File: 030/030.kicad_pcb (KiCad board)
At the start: 2 copper layers, 18 x 21.6 mm, 7 parts, among them J1 030

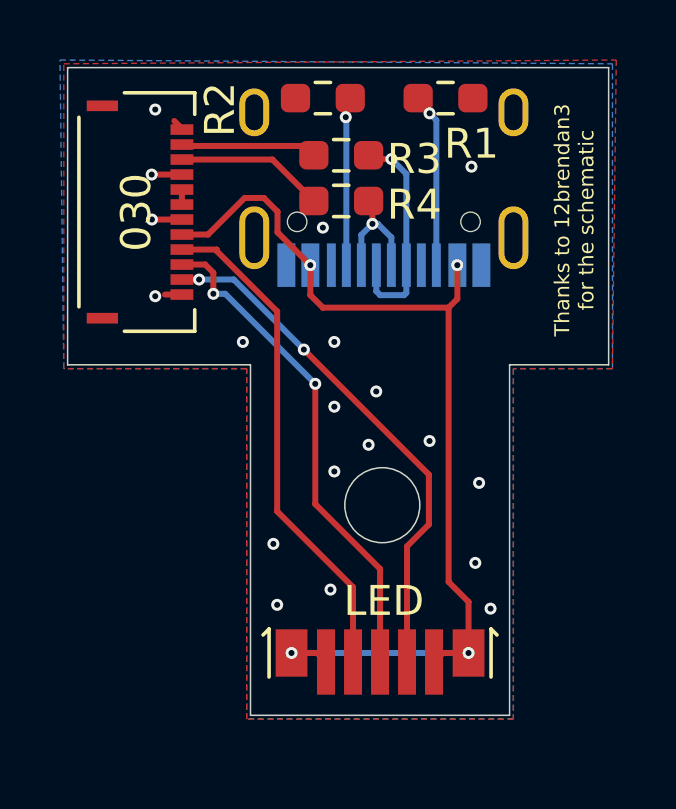
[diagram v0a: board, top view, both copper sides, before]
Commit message: update 030 to potentially correct schematic. Remove bad 001/011.
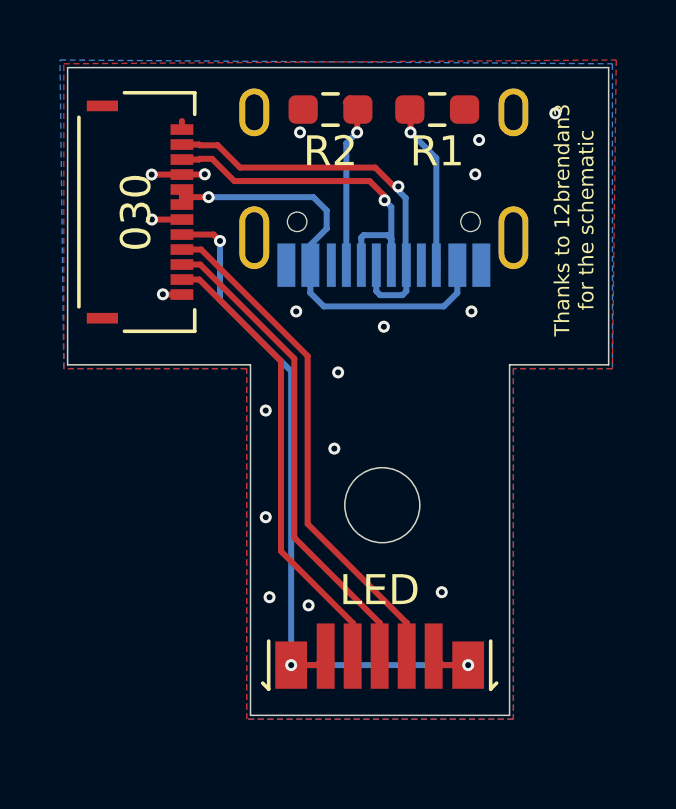
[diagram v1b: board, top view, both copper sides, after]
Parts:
- removed R3, R4: comp, Resistor_SMD:R_0603_1608Metric_Pad0.98x0.95mm_HandSolder
- moved R1 0.47 mm to (108.1, 53.7)
- moved R2 0.46 mm to (104.5, 53.7)
- moved D1 0.20 mm to (106.2, 71.9), turned to 180 degrees
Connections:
- D1 pad 1: +5V -> /Annode
- D1 pad 2: +5V -> /Annode
- D1 pad 6: +5V -> /Annode
- D1 pad 7: +5V -> /Annode
- J1 pad 5: Net-(J1-Pad5) -> +5V
- J1 pad 6: Net-(J1-Pad5) -> +5V
- J1 pad 8: +5V -> /Annode
- USB pad A6: Net-(J2-PadA6) -> /D+
- USB pad A7: Net-(J2-PadA7) -> /D-
- USB pad B6: Net-(J2-PadA6) -> /D+
- USB pad B7: Net-(J2-PadA7) -> /D-
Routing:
- net /Annode: track 0.00 -> 24.9 mm, vias 0 -> 3
- net +5V: track 33.7 -> 14.9 mm, vias 4 -> 1
- net /D+: track 4.55 -> 13.4 mm, vias 0 -> 1
- net /D-: track 4.97 -> 12.6 mm, vias 0 -> 1
- net Net-(J2-PadA6): track 7.44 -> 0.00 mm, vias 1 -> 0
- net Net-(J2-PadA7): track 4.11 -> 0.00 mm, vias 1 -> 0
- net /B: track 17.5 -> 15.5 mm, vias 2 -> 0
- net GND: track 2.96 -> 3.73 mm, vias 19 -> 18
- net Net-(J1-Pad5): track 0.50 -> 0.00 mm
- net /R: track 16.7 -> 16.3 mm, vias 2 -> 0

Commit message: 001, 011, 030 standardized to a cheaper LED
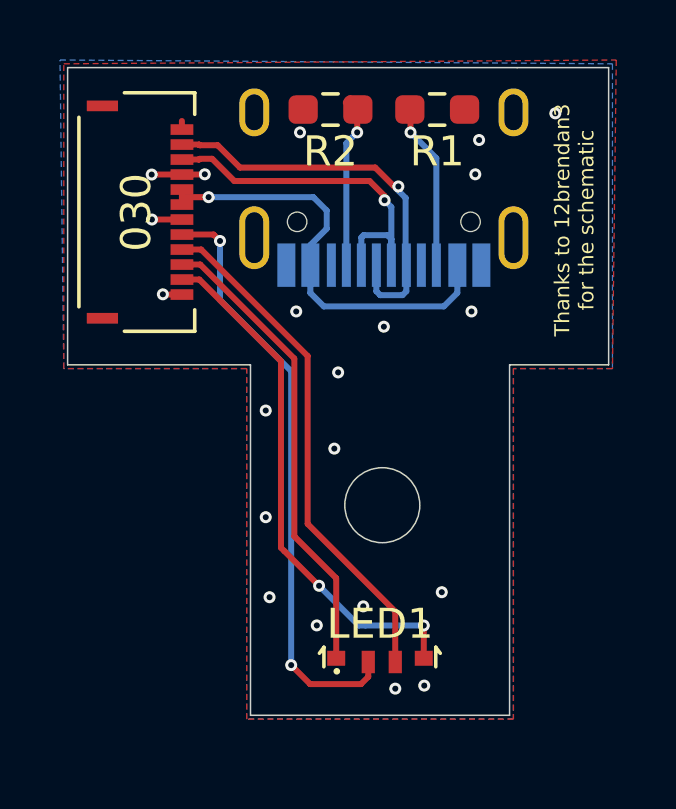
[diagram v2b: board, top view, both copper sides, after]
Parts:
- removed D1: MSL0104RGB, MSL0104RGB:MSL0104RGB
- added LED1: LED_RAGB, New_LED:FM-3510RGBA-SG, F.Cu at (106.2, 72.1)
- renumbered USB to USB1
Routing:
- net /Annode: track 24.9 -> 19.9 mm, vias 3 -> 2
- net /B: track 15.5 -> 17.6 mm, vias 0 -> 2
- net /R: track 16.3 -> 15.6 mm
- net GND: vias 18 -> 21

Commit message: 030 minor rework and gerber update
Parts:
- renumbered LED1 to LED, USB1 to USB
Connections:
- USB pad A8: Net-(USB1-PadA8) -> unconnected-(USB1-PadA8)
- USB pad B8: Net-(USB1-PadB8) -> unconnected-(USB1-PadB8)
- USB pad S1: GND -> unconnected-(USB1-PadS1)
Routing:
- net GND: track 3.73 -> 3.44 mm, vias 21 -> 31
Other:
- net class Default removed
- board text added: "JDS-030 V1.2"
- board text added: "www.casualcoders.dev"
